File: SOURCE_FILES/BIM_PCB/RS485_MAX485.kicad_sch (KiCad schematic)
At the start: 13 parts, among them U4 TBU-CA065-200-WH, U5 MAX485E, U6 TBU-CA065-200-WH

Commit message: updates on schematic and complete layout
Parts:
- removed R40: 10K, Resistor_SMD:R_0402_1005Metric, symbol Device:R_US
- added R31, R32: 100K, Resistor_SMD:R_0402_1005Metric, symbol Device:R_US
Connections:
- net +3.3VA: now also R31.2
- net GND: now also R32.1
- net B_to_CANH: now reaches R37.1, U5.7 (B)
- net A_to_CANL: now reaches R39.1, U5.6 (A)
- net RS485_EN renamed RS485_DE
- net RS485_DE: now also R32.2; no longer U5.2 (~{RE})
- new net RS485_~{RE}: R31.1, U5.2 (~{RE})
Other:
- moved on the sheet: C30, C31, C32

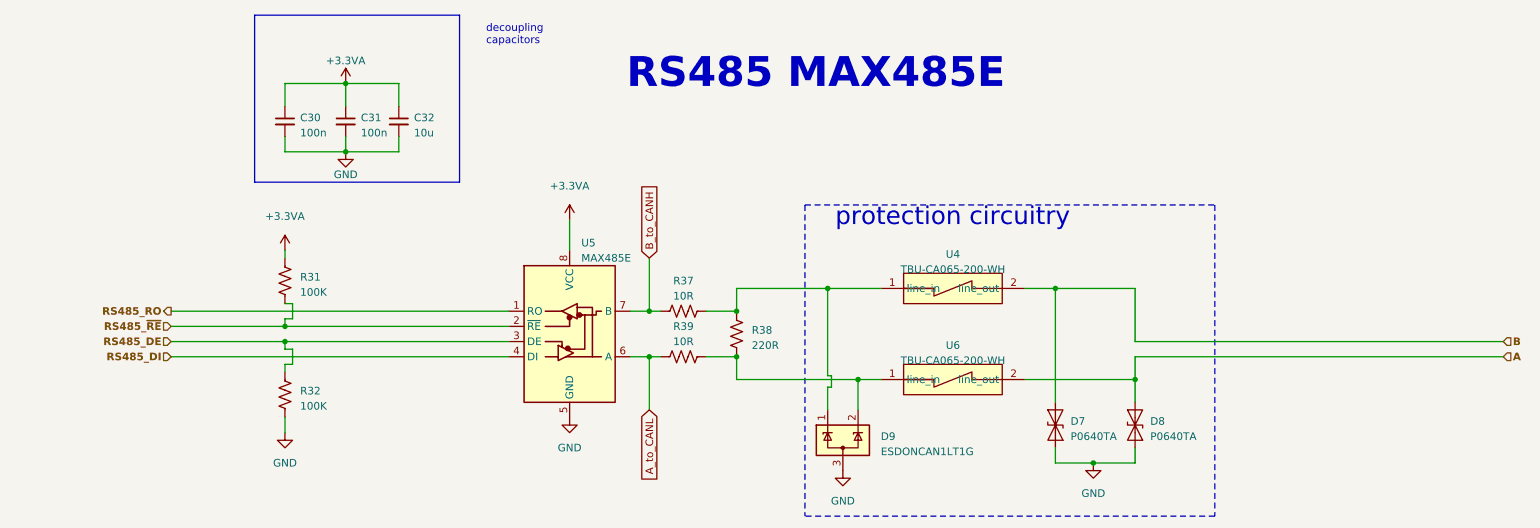
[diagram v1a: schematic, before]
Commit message: completed design PCN and Images
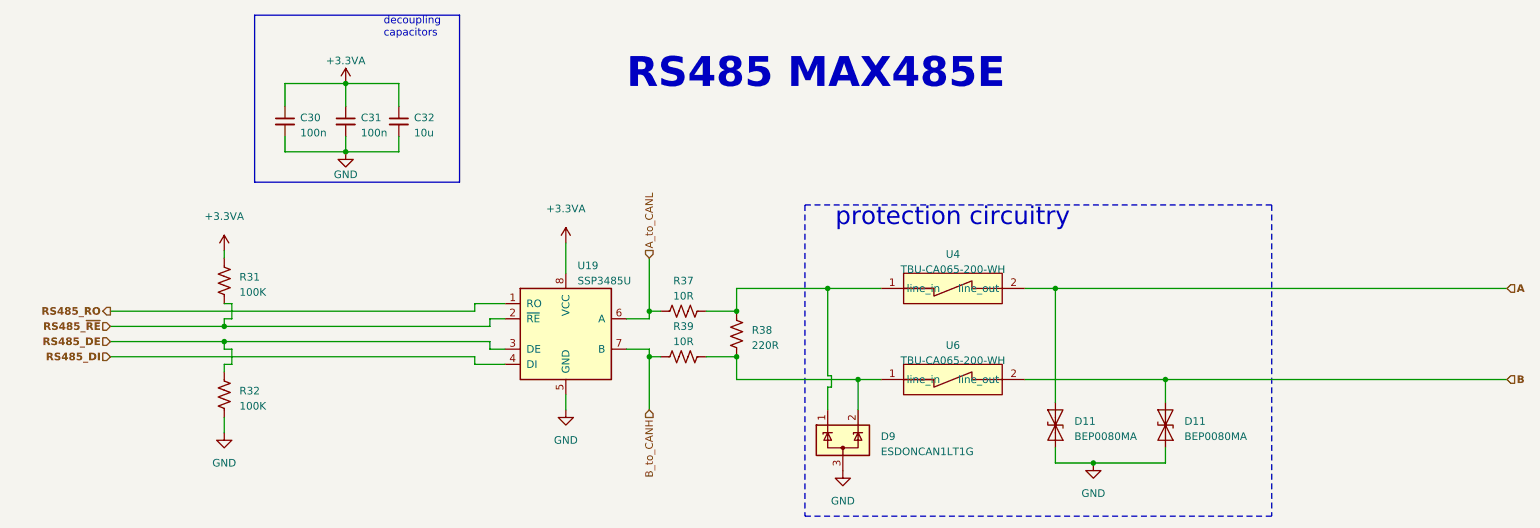
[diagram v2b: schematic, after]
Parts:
- removed D7, D8: P0640TA, Diode_SMD:D_SMA, symbol Diode:SD05_SOD323
- removed U5: MAX485E, Package_SO:SOP-8_3.9x4.9mm_P1.27mm, symbol Interface_UART:MAX485E
- added D11 (x2): BEP0080MA, Diode_SMD:D_SOD-123, symbol Diode:SD05_SOD323
- added U19: SSP3485U, Package_SO:MSOP-8_3x3mm_P0.65mm, symbol Interface_UART:SP3481CN
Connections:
- net +3.3VA: now also U19.8 (VCC)
- net A: now also U4.2 (line_out), D11.2 (A2); no longer U6.2 (line_out)
- net A_to_CANL: now also R37.1, U19.6 (A); no longer R39.1
- net B: now also U6.2 (line_out), D11.2 (A2); no longer U4.2 (line_out)
- net B_to_CANH: now also R39.1, U19.7 (B); no longer R37.1
- net GND: now also D11.1 (A1), D11.1 (A1), U19.5 (GND)
- net RS485_DE: now also U19.3 (DE)
- net RS485_DI: now also U19.4 (DI)
- net RS485_RO: now also U19.1 (RO)
- net RS485_~{RE}: now also U19.2 (~{RE})
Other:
- moved on the sheet: R31, R32

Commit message: all items updated
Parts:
- removed U4, U6: TBU-CA065-200-WH, MACHADA_footprints:TBU-CA065-200-WH, symbol MCD_General:TBU-CA065-200-WH
- added L3, L7: ferrite bead, Inductor_SMD:L_0402_1005Metric, symbol Device:L
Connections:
- net A: now also L3.2
- net B: now also L7.2
- net at D9.1 (K), R37.2, R38.2: now also L3.1
- net at D9.2 (K), R38.1, R39.2: now also L7.1
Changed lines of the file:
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@@
     (stroke (width 0) (type dash_dot))
   )
-  (wire (pts (xy 183.515 87.63) (xy 188.595 87.63))
+  (wire (pts (xy 167.005 87.63) (xy 188.595 87.63))
     (stroke (width 0) (type default))
   )
@@
     (stroke (width 0) (type default))
   )
-  (wire (pts (xy 183.515 102.87) (xy 207.01 102.87))
+  (wire (pts (xy 167.005 102.87) (xy 207.01 102.87))
     (stroke (width 0) (type default))
   )
@@
     (effects (font (size 1.27 1.27)) (justify left))
   )
+  (symbol (lib_id "Device:L") (at 163.195 102.87 90) (unit 1)
+    (in_bom yes) (on_board yes) (dnp no) (fields_autoplaced)
+    (property "Reference" "L7" (at 163.195 97.79 90)
+      (effects (font (size 1.27 1.27)))
+    )
+    (property "Value" "ferrite bead" (at 163.195 100.33 90)
+      (effects (font (size 1.27 1.27)))
+    )
+    (property "Footprint" "Inductor_SMD:L_0402_1005Metric" (at 163.195 102.87 0)
+      (effects (font (size 1.27 1.27)) hide)
+    )
+    (property "Datasheet" "~" (at 163.195 102.87 0)
+      (effects (font (size 1.27 1.27)) hide)
+    )
+    (pin "1")
+    (pin "2")
+    (instances
+      (project "BIM_PCB"
+        (path "/b79ebed7-e146-448b-8dab-0aefb3e182ca/1465f310-1de3-424a-8f4a-a980ed628081"
+          (reference "L7") (unit 1)
+        )
+        (path "/b79ebed7-e146-448b-8dab-0aefb3e182ca/34e5006d-2f61-4d7d-acbf-5a24a5d8c7fc"
+          (reference "L8") (unit 1)
+        )
+        (path "/b79ebed7-e146-448b-8dab-0aefb3e182ca/2e21452f-cdd1-4ce6-a8e8-98e1abc18b72"
+          (reference "L9") (unit 1)
+        )
+      )
+    )
+  )
   (symbol (lib_id "power:GND") (at 49.53 111.76 0) (unit 1)
     (in_bom yes) (on_board yes) (dnp no) (fields_autoplaced)
@@
     )
   )
-  (symbol (lib_id "MCD_General:TBU-CA065-200-WH") (at 169.545 82.55 0) (unit 1)
-    (in_bom yes) (on_board yes) (dnp no) (fields_autoplaced)
-    (property "Reference" "U4" (at 171.45 81.915 0)
-      (effects (font (size 1.27 1.27)))
-    )
-    (property "Value" "TBU-CA065-200-WH" (at 171.45 84.455 0)
-      (effects (font (size 1.27 1.27)))
-    )
-    (property "Footprint" "MACHADA_footprints:TBU-CA065-200-WH" (at 169.545 83.82 0)
-      (effects (font (size 1.27 1.27)) hide)
-    )
-    (property "Datasheet" "" (at 169.545 83.82 0)
-      (effects (font (size 1.27 1.27)) hide)
-    )
-    (pin "1")
-    (pin "2")
-    (instances
-      (project "BIM_PCB"
-        (path "/b79ebed7-e146-448b-8dab-0aefb3e182ca/1465f310-1de3-424a-8f4a-a980ed628081"
-          (reference "U4") (unit 1)
-        )
-        (path "/b79ebed7-e146-448b-8dab-0aefb3e182ca/34e5006d-2f61-4d7d-acbf-5a24a5d8c7fc"
-          (reference "U10") (unit 1)
-        )
-        (path "/b79ebed7-e146-448b-8dab-0aefb3e182ca/2e21452f-cdd1-4ce6-a8e8-98e1abc18b72"
-          (reference "U18") (unit 1)
-        )
-      )
-      (project "MAX485"
-        (path "/bc82bdd3-8c90-4895-abd4-de755b621eab"
-          (reference "U13") (unit 1)
-        )
-      )
-      (project "ELIESTER_V2"
-        (path "/efe55700-0211-4481-aa01-7a7eb74def17/d62e2e8a-503b-4c7c-a2bb-b074e6b71fb0"
-          (reference "U13") (unit 1)
-        )
-      )
-    )
-  )
   (symbol (lib_id "Device:R_US") (at 49.53 86.36 180) (unit 1)
     (in_bom yes) (on_board yes) (dnp no) (fields_autoplaced)
@@
         (path "/efe55700-0211-4481-aa01-7a7eb74def17/d62e2e8a-503b-4c7c-a2bb-b074e6b71fb0"
           (reference "#PWR089") (unit 1)
-        )
-      )
-    )
-  )
-  (symbol (lib_id "MCD_General:TBU-CA065-200-WH") (at 169.545 97.79 0) (unit 1)
-    (in_bom yes) (on_board yes) (dnp no) (fields_autoplaced)
-    (property "Reference" "U6" (at 171.45 97.155 0)
-      (effects (font (size 1.27 1.27)))
-    )
-    (property "Value" "TBU-CA065-200-WH" (at 171.45 99.695 0)
-      (effects (font (size 1.27 1.27)))
-    )
-    (property "Footprint" "MACHADA_footprints:TBU-CA065-200-WH" (at 169.545 99.06 0)
-      (effects (font (size 1.27 1.27)) hide)
-    )
-    (property "Datasheet" "" (at 169.545 99.06 0)
-      (effects (font (size 1.27 1.27)) hide)
-    )
-    (pin "1")
-    (pin "2")
-    (instances
-      (project "BIM_PCB"
-        (path "/b79ebed7-e146-448b-8dab-0aefb3e182ca/1465f310-1de3-424a-8f4a-a980ed628081"
-          (reference "U6") (unit 1)
-        )
-        (path "/b79ebed7-e146-448b-8dab-0aefb3e182ca/34e5006d-2f61-4d7d-acbf-5a24a5d8c7fc"
-          (reference "U12") (unit 1)
-        )
-        (path "/b79ebed7-e146-448b-8dab-0aefb3e182ca/2e21452f-cdd1-4ce6-a8e8-98e1abc18b72"
-          (reference "U20") (unit 1)
-        )
-      )
-      (project "MAX485"
-        (path "/bc82bdd3-8c90-4895-abd4-de755b621eab"
-          (reference "U16") (unit 1)
-        )
-      )
-      (project "ELIESTER_V2"
-        (path "/efe55700-0211-4481-aa01-7a7eb74def17/d62e2e8a-503b-4c7c-a2bb-b074e6b71fb0"
-          (reference "U16") (unit 1)
         )
       )
@@
         )
       )
+    )
+  )
+  (symbol (lib_id "Device:L") (at 163.195 87.63 90) (unit 1)
+    (in_bom yes) (on_board yes) (dnp no) (fields_autoplaced)
+    (property "Reference" "L3" (at 163.195 82.55 90)
+      (effects (font (size 1.27 1.27)))
+    )
+    (property "Value" "ferrite bead" (at 163.195 85.09 90)
+      (effects (font (size 1.27 1.27)))
+    )
+    (property "Footprint" "Inductor_SMD:L_0402_1005Metric" (at 163.195 87.63 0)
+      (effects (font (size 1.27 1.27)) hide)
+    )
+    (property "Datasheet" "~" (at 163.195 87.63 0)
+      (effects (font (size 1.27 1.27)) hide)
+    )
+    (pin "1")
+    (pin "2")
+    (instances
+      (project "BIM_PCB"
+        (path "/b79ebed7-e146-448b-8dab-0aefb3e182ca/1465f310-1de3-424a-8f4a-a980ed628081"
+          (reference "L3") (unit 1)
+        )
+        (path "/b79ebed7-e146-448b-8dab-0aefb3e182ca/34e5006d-2f61-4d7d-acbf-5a24a5d8c7fc"
+          (reference "L4") (unit 1)
+        )
+        (path "/b79ebed7-e146-448b-8dab-0aefb3e182ca/2e21452f-cdd1-4ce6-a8e8-98e1abc18b72"
+          (reference "L6") (unit 1)
+        )
+      )
